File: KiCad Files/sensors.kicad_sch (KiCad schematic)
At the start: 0 parts

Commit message: hall1
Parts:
- added IC? (x4): AH1902-Z-7, AH1902Z7, symbol AH1902-Z-7:AH1902-Z-7
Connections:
- new net 3.3V: IC?.4 (VDD), IC?.4 (VDD), IC?.4 (VDD), IC?.4 (VDD)
- new net GND: IC?.1 (NC_1), IC?.1 (NC_1), IC?.1 (NC_1), IC?.1 (NC_1), IC?.2 (GND), IC?.2 (GND), IC?.2 (GND), IC?.2 (GND), IC?.3 (NC_2), IC?.3 (NC_2), IC?.3 (NC_2), IC?.3 (NC_2)

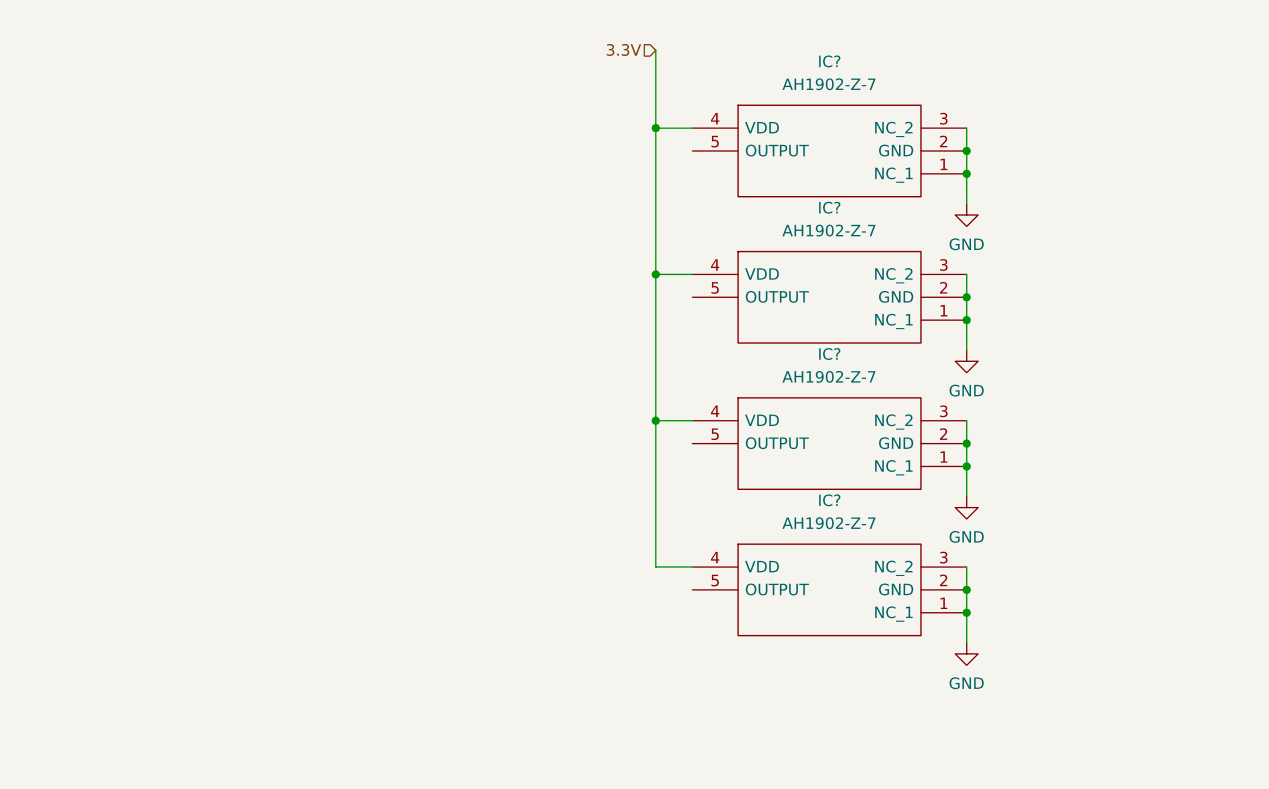
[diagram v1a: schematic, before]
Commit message: Hall sensors mux
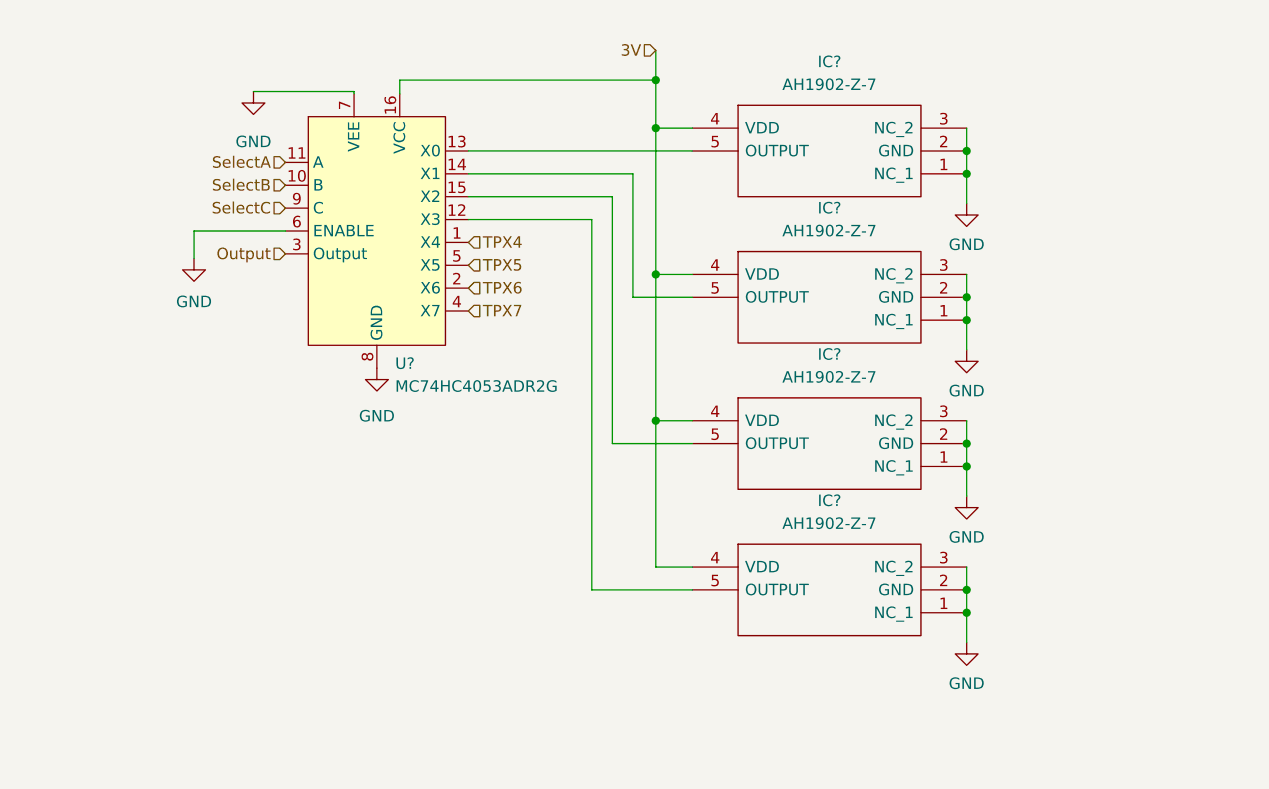
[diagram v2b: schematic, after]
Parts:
- added U?: MC74HC4053ADR2G, symbol mc74hc4053adr2g:MC74HC4053ADR2G
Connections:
- net GND: now also U?.6 (ENABLE), U?.7 (VEE), U?.8 (GND)
- net at IC?.5 (OUTPUT): now also U?.14 (X1)
- net at IC?.5 (OUTPUT): now also U?.12 (X3)
- net at IC?.5 (OUTPUT): now also U?.15 (X2)
- net at IC?.5 (OUTPUT): now also U?.13 (X0)
- net 3.3V renamed 3V
- net 3V: now also U?.16 (VCC)
- new net Output: U?.3 (Output)
- new net SelectA: U?.11 (A)
- new net SelectB: U?.10 (B)
- new net SelectC: U?.9 (C)
- new net TPX4: U?.1 (X4)
- new net TPX5: U?.5 (X5)
- new net TPX6: U?.2 (X6)
- new net TPX7: U?.4 (X7)
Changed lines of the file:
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@@
   (junction (at 130.556 62.992) (diameter 0) (color 0 0 0 0)
   )
+  (junction (at 130.556 41.402) (diameter 0) (color 0 0 0 0)
+  )
   (junction (at 165.1 51.816) (diameter 0) (color 0 0 0 0)
   )
@@
   (junction (at 130.556 46.736) (diameter 0) (color 0 0 0 0)
   )
-  (wire (pts (xy 130.556 38.1) (xy 130.556 46.736))
+  (wire (pts (xy 109.728 54.356) (xy 125.73 54.356))
+    (stroke (width 0) (type default) (color 0 0 0 0))
+  )
+  (wire (pts (xy 109.728 49.276) (xy 134.62 49.276))
+    (stroke (width 0) (type default) (color 0 0 0 0))
+  )
+  (wire (pts (xy 109.728 56.896) (xy 123.444 56.896))
+    (stroke (width 0) (type default) (color 0 0 0 0))
+  )
+  (wire (pts (xy 130.556 38.1) (xy 130.556 41.402))
+    (stroke (width 0) (type default) (color 0 0 0 0))
+  )
+  (wire (pts (xy 85.852 42.672) (xy 97.028 42.672))
+    (stroke (width 0) (type default) (color 0 0 0 0))
+  )
+  (wire (pts (xy 97.028 42.672) (xy 97.028 42.926))
     (stroke (width 0) (type default) (color 0 0 0 0))
   )
@@
     (stroke (width 0) (type default) (color 0 0 0 0))
   )
+  (wire (pts (xy 102.108 41.402) (xy 130.556 41.402))
+    (stroke (width 0) (type default) (color 0 0 0 0))
+  )
+  (wire (pts (xy 79.248 58.166) (xy 89.408 58.166))
+    (stroke (width 0) (type default) (color 0 0 0 0))
+  )
+  (wire (pts (xy 128.016 65.532) (xy 134.62 65.532))
+    (stroke (width 0) (type default) (color 0 0 0 0))
+  )
   (wire (pts (xy 130.556 79.248) (xy 130.556 95.504))
     (stroke (width 0) (type default) (color 0 0 0 0))
@@
     (stroke (width 0) (type default) (color 0 0 0 0))
   )
+  (wire (pts (xy 102.108 42.926) (xy 102.108 41.402))
+    (stroke (width 0) (type default) (color 0 0 0 0))
+  )
+  (wire (pts (xy 109.728 51.816) (xy 128.016 51.816))
+    (stroke (width 0) (type default) (color 0 0 0 0))
+  )
   (wire (pts (xy 165.1 68.072) (xy 165.1 71.374))
     (stroke (width 0) (type default) (color 0 0 0 0))
   )
+  (wire (pts (xy 125.73 81.788) (xy 134.62 81.788))
+    (stroke (width 0) (type default) (color 0 0 0 0))
+  )
   (wire (pts (xy 130.556 62.992) (xy 134.62 62.992))
     (stroke (width 0) (type default) (color 0 0 0 0))
   )
+  (wire (pts (xy 123.444 56.896) (xy 123.444 98.044))
+    (stroke (width 0) (type default) (color 0 0 0 0))
+  )
   (wire (pts (xy 165.1 79.248) (xy 165.1 81.788))
     (stroke (width 0) (type default) (color 0 0 0 0))
@@
     (stroke (width 0) (type default) (color 0 0 0 0))
   )
+  (wire (pts (xy 128.016 51.816) (xy 128.016 65.532))
+    (stroke (width 0) (type default) (color 0 0 0 0))
+  )
   (wire (pts (xy 165.1 81.788) (xy 165.1 84.328))
     (stroke (width 0) (type default) (color 0 0 0 0))
   )
+  (wire (pts (xy 123.444 98.044) (xy 134.62 98.044))
+    (stroke (width 0) (type default) (color 0 0 0 0))
+  )
+  (wire (pts (xy 130.556 41.402) (xy 130.556 46.736))
+    (stroke (width 0) (type default) (color 0 0 0 0))
+  )
   (wire (pts (xy 165.1 62.992) (xy 165.1 65.532))
     (stroke (width 0) (type default) (color 0 0 0 0))
@@
     (stroke (width 0) (type default) (color 0 0 0 0))
   )
+  (wire (pts (xy 125.73 54.356) (xy 125.73 81.788))
+    (stroke (width 0) (type default) (color 0 0 0 0))
+  )
   (wire (pts (xy 130.556 79.248) (xy 134.62 79.248))
     (stroke (width 0) (type default) (color 0 0 0 0))
   )
+  (wire (pts (xy 79.248 61.214) (xy 79.248 58.166))
+    (stroke (width 0) (type default) (color 0 0 0 0))
+  )
   (wire (pts (xy 130.556 46.736) (xy 130.556 62.992))
     (stroke (width 0) (type default) (color 0 0 0 0))
   )
-  (hierarchical_label "3.3V" (shape input) (at 130.556 38.1 180)
-    (effects (font (size 1.27 1.27)) (justify right))
+  (hierarchical_label "Output" (shape input) (at 89.408 60.706 180)
+    (effects (font (size 1.27 1.27)) (justify right))
+  )
+  (hierarchical_label "TPX7" (shape input) (at 109.728 67.056 0)
+    (effects (font (size 1.27 1.27)) (justify left))
+  )
+  (hierarchical_label "TPX4" (shape input) (at 109.728 59.436 0)
+    (effects (font (size 1.27 1.27)) (justify left))
+  )
+  (hierarchical_label "3V" (shape input) (at 130.556 38.1 180)
+    (effects (font (size 1.27 1.27)) (justify right))
+  )
+  (hierarchical_label "SelectB" (shape input) (at 89.408 53.086 180)
+    (effects (font (size 1.27 1.27)) (justify right))
+  )
+  (hierarchical_label "TPX6" (shape input) (at 109.728 64.516 0)
+    (effects (font (size 1.27 1.27)) (justify left))
+  )
+  (hierarchical_label "SelectA" (shape input) (at 89.408 50.546 180)
+    (effects (font (size 1.27 1.27)) (justify right))
+  )
+  (hierarchical_label "SelectC" (shape input) (at 89.408 55.626 180)
+    (effects (font (size 1.27 1.27)) (justify right))
+  )
+  (hierarchical_label "TPX5" (shape input) (at 109.728 61.976 0)
+    (effects (font (size 1.27 1.27)) (justify left))
   )
   (symbol (lib_id "AH1902-Z-7:AH1902-Z-7") (at 134.62 62.992 0) (unit 1)
@@
     (pin "5")
   )
+  (symbol (lib_id "power:GND") (at 79.248 61.214 0) (unit 1)
+    (in_bom yes) (on_board yes) (fields_autoplaced)
+    (property "Reference" "#PWR?" (id 0) (at 79.248 67.564 0)
+      (effects (font (size 1.27 1.27)) hide)
+    )
+    (property "Value" "GND" (id 1) (at 79.248 66.04 0))
+    (property "Footprint" "" (id 2) (at 79.248 61.214 0)
+      (effects (font (size 1.27 1.27)) hide)
+    )
+    (property "Datasheet" "" (id 3) (at 79.248 61.214 0)
+      (effects (font (size 1.27 1.27)) hide)
+    )
+    (pin "1")
+  )
   (symbol (lib_id "AH1902-Z-7:AH1902-Z-7") (at 134.62 95.504 0) (unit 1)
     (in_bom yes) (on_board yes) (fields_autoplaced)
@@
     (pin "5")
   )
+  (symbol (lib_id "power:GND") (at 85.852 42.672 0) (unit 1)
+    (in_bom yes) (on_board yes) (fields_autoplaced)
+    (property "Reference" "#PWR?" (id 0) (at 85.852 49.022 0)
+      (effects (font (size 1.27 1.27)) hide)
+    )
+    (property "Value" "GND" (id 1) (at 85.852 48.26 0))
+    (property "Footprint" "" (id 2) (at 85.852 42.672 0)
+      (effects (font (size 1.27 1.27)) hide)
+    )
+    (property "Datasheet" "" (id 3) (at 85.852 42.672 0)
+      (effects (font (size 1.27 1.27)) hide)
+    )
+    (pin "1")
+  )
   (symbol (lib_id "power:GND") (at 165.1 71.374 0) (unit 1)
     (in_bom yes) (on_board yes) (fields_autoplaced)
@@
       (effects (font (size 1.27 1.27)) hide)
     )
+    (pin "1")
+  )
+  (symbol (lib_id "mc74hc4053adr2g:MC74HC4053ADR2G") (at 99.568 59.436 0) (unit 1)
+    (in_bom yes) (on_board yes) (fields_autoplaced)
+    (property "Reference" "U?" (id 0) (at 101.5874 72.898 0)
+      (effects (font (size 1.27 1.27)) (justify left))
+    )
+    (property "Value" "MC74HC4053ADR2G" (id 1) (at 101.5874 75.438 0)
+      (effects (font (size 1.27 1.27)) (justify left))
+    )
+    (property "Footprint" "" (id 2) (at 99.568 59.436 0)
+      (effects (font (size 1.27 1.27)) hide)
+    )
+    (property "Datasheet" "" (id 3) (at 99.568 59.436 0)
+      (effects (font (size 1.27 1.27)) hide)
+    )
+    (pin "1")
+    (pin "10")
+    (pin "11")
+    (pin "12")
+    (pin "13")
+    (pin "14")
+    (pin "15")
+    (pin "16")
+    (pin "2")
+    (pin "3")
+    (pin "4")
+    (pin "5")
+    (pin "6")
+    (pin "7")
+    (pin "8")
+    (pin "9")
+  )
+  (symbol (lib_id "power:GND") (at 99.568 73.406 0) (unit 1)
+    (in_bom yes) (on_board yes) (fields_autoplaced)
+    (property "Reference" "#PWR?" (id 0) (at 99.568 79.756 0)
+      (effects (font (size 1.27 1.27)) hide)
+    )
+    (property "Value" "GND" (id 1) (at 99.568 78.74 0))
+    (property "Footprint" "" (id 2) (at 99.568 73.406 0)
+      (effects (font (size 1.27 1.27)) hide)
+    )
+    (property "Datasheet" "" (id 3) (at 99.568 73.406 0)
+      (effects (font (size 1.27 1.27)) hide)
+    )

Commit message: Sensors Done
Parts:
- removed U?: MC74HC4053ADR2G, symbol mc74hc4053adr2g:MC74HC4053ADR2G
- added C1, C2, C3, C4: C, symbol Device:C
- added U2: 74HC165, symbol 74xx:74HC165
- gave numbers to parts that had none: 4
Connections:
- net 3V: now also C1.1, C2.1, C3.1, C4.1
- net GND: now also C1.2, C2.2, C3.2, C4.2, U2.10 (DS), U2.3 (D4), U2.4 (D5), U2.5 (D6), U2.6 (D7), U2.8 (GND)
- net at IC2.5 (OUTPUT): now also U2.12 (D1)
- net at IC4.5 (OUTPUT): now also U2.14 (D3)
- net at IC3.5 (OUTPUT): now also U2.13 (D2)
- net at IC1.5 (OUTPUT): now also U2.11 (D0)
- new net 5V: U2.16 (VCC)
- new net ClkEnIn: U2.15 (~{CE})
- new net ClkIn: U2.2 (CP)
- new net NPL: U2.1 (~{PL})
- new net NSEROutput: U2.7 (~{Q7})
- new net SEROutput: U2.9 (Q7)
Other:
- moved on the sheet: IC1, IC2, IC3, IC4

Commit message: Added footprints
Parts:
- U2: footprint (none) -> 74HC165:SO-16; JLC Part Number (none) -> C5613
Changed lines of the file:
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@@
       (effects (font (size 1.27 1.27)) (justify right))
     )
-    (property "Footprint" "" (id 2) (at 97.028 61.976 0)
+    (property "Footprint" "74HC165:SO-16" (id 2) (at 97.028 61.976 0)
       (effects (font (size 1.27 1.27)) hide)
     )
-    (property "Datasheet" "https://assets.nexperia.com/documents/data-sheet/74HC_HCT165.pdf" (id 3) (at 97.028 61.976 0)
+    (property "Datasheet" "https://datasheet.lcsc.com/lcsc/1811021715_Nexperia-74HC165D-653_C5613.pdf" (id 3) (at 97.028 61.976 0)
       (effects (font (size 1.27 1.27)) hide)
     )
+    (property "JLC Part Number" "C5613" (id 4) (at 97.028 61.976 0)
+      (effects (font (size 1.27 1.27)) hide)
+    )

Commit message: More footprints
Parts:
- C1, C2, C3, C4: value C -> 0.1u; footprint (none) -> Capacitor_SMD:C_0402_1005Metric; JLC Part Number (none) -> C1525
- IC1, IC2, IC3, IC4: JLC Part Number (none) -> C239188
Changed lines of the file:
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@@
       (effects (font (size 1.27 1.27)) (justify left))
     )
-    (property "Value" "C" (id 1) (at 142.24 106.4259 0)
-      (effects (font (size 1.27 1.27)) (justify left))
-    )
-    (property "Footprint" "" (id 2) (at 139.3952 108.966 0)
-      (effects (font (size 1.27 1.27)) hide)
-    )
-    (property "Datasheet" "~" (id 3) (at 138.43 105.156 0)
+    (property "Value" "0.1u" (id 1) (at 142.24 106.4259 0)
+      (effects (font (size 1.27 1.27)) (justify left))
+    )
+    (property "Footprint" "Capacitor_SMD:C_0402_1005Metric" (id 2) (at 139.3952 108.966 0)
+      (effects (font (size 1.27 1.27)) hide)
+    )
+    (property "Datasheet" "https://datasheet.lcsc.com/lcsc/1810191219_Samsung-Electro-Mechanics-CL05B104KO5NNNC_C1525.pdf" (id 3) (at 138.43 105.156 0)
+      (effects (font (size 1.27 1.27)) hide)
+    )
+    (property "JLC Part Number" "C1525" (id 4) (at 138.43 105.156 0)
       (effects (font (size 1.27 1.27)) hide)
     )
@@
       (effects (font (size 1.27 1.27)) (justify left) hide)
     )
+    (property "JLC Part Number" "C239188" (id 12) (at 141.478 62.992 0)
+      (effects (font (size 1.27 1.27)) hide)
+    )
     (pin "1")
     (pin "2")
@@
       (effects (font (size 1.27 1.27)) (justify left))
     )
-    (property "Value" "C" (id 1) (at 141.732 56.8959 0)
-      (effects (font (size 1.27 1.27)) (justify left))
-    )
-    (property "Footprint" "" (id 2) (at 138.8872 59.436 0)
-      (effects (font (size 1.27 1.27)) hide)
-    )
-    (property "Datasheet" "~" (id 3) (at 137.922 55.626 0)
+    (property "Value" "0.1u" (id 1) (at 141.732 56.8959 0)
+      (effects (font (size 1.27 1.27)) (justify left))
+    )
+    (property "Footprint" "Capacitor_SMD:C_0402_1005Metric" (id 2) (at 138.8872 59.436 0)
+      (effects (font (size 1.27 1.27)) hide)
+    )
+    (property "Datasheet" "https://datasheet.lcsc.com/lcsc/1810191219_Samsung-Electro-Mechanics-CL05B104KO5NNNC_C1525.pdf" (id 3) (at 137.922 55.626 0)
+      (effects (font (size 1.27 1.27)) hide)
+    )
+    (property "JLC Part Number" "C1525" (id 4) (at 137.922 55.626 0)
       (effects (font (size 1.27 1.27)) hide)
     )
@@
       (effects (font (size 1.27 1.27)) (justify left))
     )
-    (property "Value" "C" (id 1) (at 141.732 89.1539 0)
-      (effects (font (size 1.27 1.27)) (justify left))
-    )
-    (property "Footprint" "" (id 2) (at 138.8872 91.694 0)
-      (effects (font (size 1.27 1.27)) hide)
-    )
-    (property "Datasheet" "~" (id 3) (at 137.922 87.884 0)
+    (property "Value" "0.1u" (id 1) (at 141.732 89.1539 0)
+      (effects (font (size 1.27 1.27)) (justify left))
+    )
+    (property "Footprint" "Capacitor_SMD:C_0402_1005Metric" (id 2) (at 138.8872 91.694 0)
+      (effects (font (size 1.27 1.27)) hide)
+    )
+    (property "Datasheet" "https://datasheet.lcsc.com/lcsc/1810191219_Samsung-Electro-Mechanics-CL05B104KO5NNNC_C1525.pdf" (id 3) (at 137.922 87.884 0)
+      (effects (font (size 1.27 1.27)) hide)
+    )
+    (property "JLC Part Number" "C1525" (id 4) (at 137.922 87.884 0)
       (effects (font (size 1.27 1.27)) hide)
     )
@@
       (effects (font (size 1.27 1.27)) (justify left) hide)
     )
+    (property "JLC Part Number" "C239188" (id 12) (at 141.478 95.504 0)
+      (effects (font (size 1.27 1.27)) hide)
+    )
     (pin "1")
     (pin "2")
@@
       (effects (font (size 1.27 1.27)) (justify left) hide)
     )
+    (property "JLC Part Number" "C239188" (id 12) (at 141.478 79.248 0)
+      (effects (font (size 1.27 1.27)) hide)
+    )
     (pin "1")
     (pin "2")
@@
       (effects (font (size 1.27 1.27)) (justify left))
     )
-    (property "Value" "C" (id 1) (at 141.732 73.1519 0)
-      (effects (font (size 1.27 1.27)) (justify left))
-    )
-    (property "Footprint" "" (id 2) (at 138.8872 75.692 0)
-      (effects (font (size 1.27 1.27)) hide)
-    )
-    (property "Datasheet" "~" (id 3) (at 137.922 71.882 0)
+    (property "Value" "0.1u" (id 1) (at 141.732 73.1519 0)
+      (effects (font (size 1.27 1.27)) (justify left))
+    )
+    (property "Footprint" "Capacitor_SMD:C_0402_1005Metric" (id 2) (at 138.8872 75.692 0)
+      (effects (font (size 1.27 1.27)) hide)
+    )
+    (property "Datasheet" "https://datasheet.lcsc.com/lcsc/1810191219_Samsung-Electro-Mechanics-CL05B104KO5NNNC_C1525.pdf" (id 3) (at 137.922 71.882 0)
+      (effects (font (size 1.27 1.27)) hide)
+    )
+    (property "JLC Part Number" "C1525" (id 4) (at 137.922 71.882 0)
       (effects (font (size 1.27 1.27)) hide)
     )
@@
       (effects (font (size 1.27 1.27)) (justify left) hide)
     )
-    (pin "1")
+    (property "JLC Part Number" "C239188" (id 12) (at 141.478 46.736 0)
+      (effects (font (size 1.27 1.27)) hide)
+    )
+    (pin "1")

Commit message: Pcb2
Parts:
- renumbered U2 to U3
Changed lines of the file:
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@@
   (symbol (lib_id "power:GND") (at 112.014 83.566 0) (unit 1)
     (in_bom yes) (on_board yes) (fields_autoplaced)
-    (property "Reference" "#PWR07" (id 0) (at 112.014 89.916 0)
+    (property "Reference" "#PWR08" (id 0) (at 112.014 89.916 0)
       (effects (font (size 1.27 1.27)) hide)
     )
@@
   (symbol (lib_id "74xx:74HC165") (at 97.028 61.976 0) (mirror y) (unit 1)
     (in_bom yes) (on_board yes) (fields_autoplaced)
-    (property "Reference" "U2" (id 0) (at 97.5486 39.116 0)
+    (property "Reference" "U3" (id 0) (at 97.5486 39.116 0)
       (effects (font (size 1.27 1.27)) (justify right))
     )
@@
   (symbol (lib_id "power:GND") (at 97.028 87.376 0) (unit 1)
     (in_bom yes) (on_board yes) (fields_autoplaced)
-    (property "Reference" "#PWR06" (id 0) (at 97.028 93.726 0)
+    (property "Reference" "#PWR07" (id 0) (at 97.028 93.726 0)
       (effects (font (size 1.27 1.27)) hide)
     )
@@
   (symbol (lib_id "power:GND") (at 171.958 71.374 0) (unit 1)
     (in_bom yes) (on_board yes) (fields_autoplaced)
-    (property "Reference" "#PWR010" (id 0) (at 171.958 77.724 0)
+    (property "Reference" "#PWR011" (id 0) (at 171.958 77.724 0)
       (effects (font (size 1.27 1.27)) hide)
     )
@@
   (symbol (lib_id "power:GND") (at 171.958 55.118 0) (unit 1)
     (in_bom yes) (on_board yes) (fields_autoplaced)
-    (property "Reference" "#PWR09" (id 0) (at 171.958 61.468 0)
+    (property "Reference" "#PWR010" (id 0) (at 171.958 61.468 0)
       (effects (font (size 1.27 1.27)) hide)
     )
@@
   (symbol (lib_id "power:GND") (at 171.958 103.886 0) (unit 1)
     (in_bom yes) (on_board yes) (fields_autoplaced)
-    (property "Reference" "#PWR012" (id 0) (at 171.958 110.236 0)
+    (property "Reference" "#PWR013" (id 0) (at 171.958 110.236 0)
       (effects (font (size 1.27 1.27)) hide)
     )
@@
   (symbol (lib_id "power:GND") (at 138.43 112.268 0) (unit 1)
     (in_bom yes) (on_board yes) (fields_autoplaced)
-    (property "Reference" "#PWR08" (id 0) (at 138.43 118.618 0)
+    (property "Reference" "#PWR09" (id 0) (at 138.43 118.618 0)
       (effects (font (size 1.27 1.27)) hide)
     )
@@
   (symbol (lib_id "power:GND") (at 171.958 87.63 0) (unit 1)
     (in_bom yes) (on_board yes) (fields_autoplaced)
-    (property "Reference" "#PWR011" (id 0) (at 171.958 93.98 0)
-      (effects (font (size 1.27 1.27)) hide)
-    )
+    (property "Reference" "#PWR012" (id 0) (at 171.958 93.98 0)
+      (effects (font (size 1.27 1.27)) hide)
+    )
